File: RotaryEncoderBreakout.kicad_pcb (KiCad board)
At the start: 2 copper layers, 36 x 44.1 mm, 18 parts, among them J1 Conn_01x04_Male, J2 Conn_01x04_Male, J3 Conn_01x03_Male, SW1 RotaryEncoder_Switch_RGB, U1 WS2811

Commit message: Layout complete
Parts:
- removed R9: 0R, Resistors_SMD:R_0805_HandSoldering
- J1, J2: moved to F.Cu
- J3: value Conn_01x03_Male -> Conn_01x05_Male; footprint Pin_Headers:Pin_Header_Straight_1x03_Pitch2.54mm -> Pin_Headers:Pin_Header_Straight_1x05_Pitch2.54mm
- moved R7 15.6 mm to (135.9, 59.1)
- moved J1 7.65 mm to (113.7, 74.5)
- moved J2 7.65 mm to (113.7, 62.9)
- moved J3 4.58 mm to (137.2, 55.2), turned to 270 degrees
- moved C3 3.86 mm to (121.9, 59.1)
- moved R5 3.24 mm to (128.3, 84.5)
- moved SW1 2.92 mm to (132.1, 74.3)
- moved R6 2.62 mm to (118.1, 59.1), turned to 90 degrees
- moved R4 2.62 mm to (135.9, 84.5)
- moved U1 2.29 mm to (128.9, 61.0)
- moved R1 1.42 mm to (135.9, 63.5), turned to 0 degrees
- moved R2 1.27 mm to (121.9, 73.0), turned to 90 degrees
- moved R3 1.27 mm to (121.9, 79.4)
- moved R8 1.27 mm to (121.9, 66.7), turned to 90 degrees
- turned C1 to 270 degrees
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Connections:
- J1 pad 1: Net-(C4-Pad1) -> Net-(J1-Pad1)
- J1 pad 2: Net-(C1-Pad1) -> Net-(C2-Pad1)
- J1 pad 3: Net-(C2-Pad1) -> Net-(C1-Pad1)
- J1 pad 4: Net-(J1-Pad4) -> Net-(C4-Pad1)
- J2 pad 1: +5V -> Net-(J2-Pad1)
- J2 pad 4: Net-(J2-Pad4) -> +5V
- J3 pad 1: Net-(J3-Pad1) -> Net-(J1-Pad1)
- J3 pad 3: Net-(J1-Pad4) -> Net-(J3-Pad3)
- U1 pad 5: Net-(J3-Pad1) -> Net-(J3-Pad3)
- U1 pad 7: Net-(R9-Pad2) -> Net-(J3-Pad4)
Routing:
- net +5V: track 19.4 -> 95.6 mm, vias 1 -> 2
- net Net-(J1-Pad1): track 0.00 -> 50.7 mm
- net Net-(R3-Pad1): track 0.00 -> 21.7 mm
- net Net-(R1-Pad1): track 0.00 -> 18.2 mm, vias 0 -> 1
- net Net-(R2-Pad1): track 0.00 -> 13.5 mm
- net GND: track 0.00 -> 13.0 mm, vias 0 -> 7
- net Net-(C2-Pad1): track 0.00 -> 12.3 mm
- net Net-(J3-Pad1): track 10.6 -> 0.00 mm
- net Net-(C1-Pad1): track 0.00 -> 10.1 mm
- net Net-(C3-Pad2): track 0.00 -> 9.33 mm
- net Net-(C4-Pad1): track 0.00 -> 8.92 mm
- net Net-(SW1-Pad4): track 0.00 -> 7.38 mm
- net Net-(R7-Pad1): track 0.00 -> 7.01 mm
- net Net-(SW1-Pad2): track 0.00 -> 4.38 mm
- net Net-(SW1-Pad1): track 0.00 -> 4.08 mm
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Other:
- board size 36 x 44.1 mm -> 33 x 34.3 mm
- board text added: "5V"
- board text added: "GND"
- board text added: "PC0"
- board text added: "PC1"
- board text added: "PC2"
- board text added: "PC3"
- board text added: "Vin"

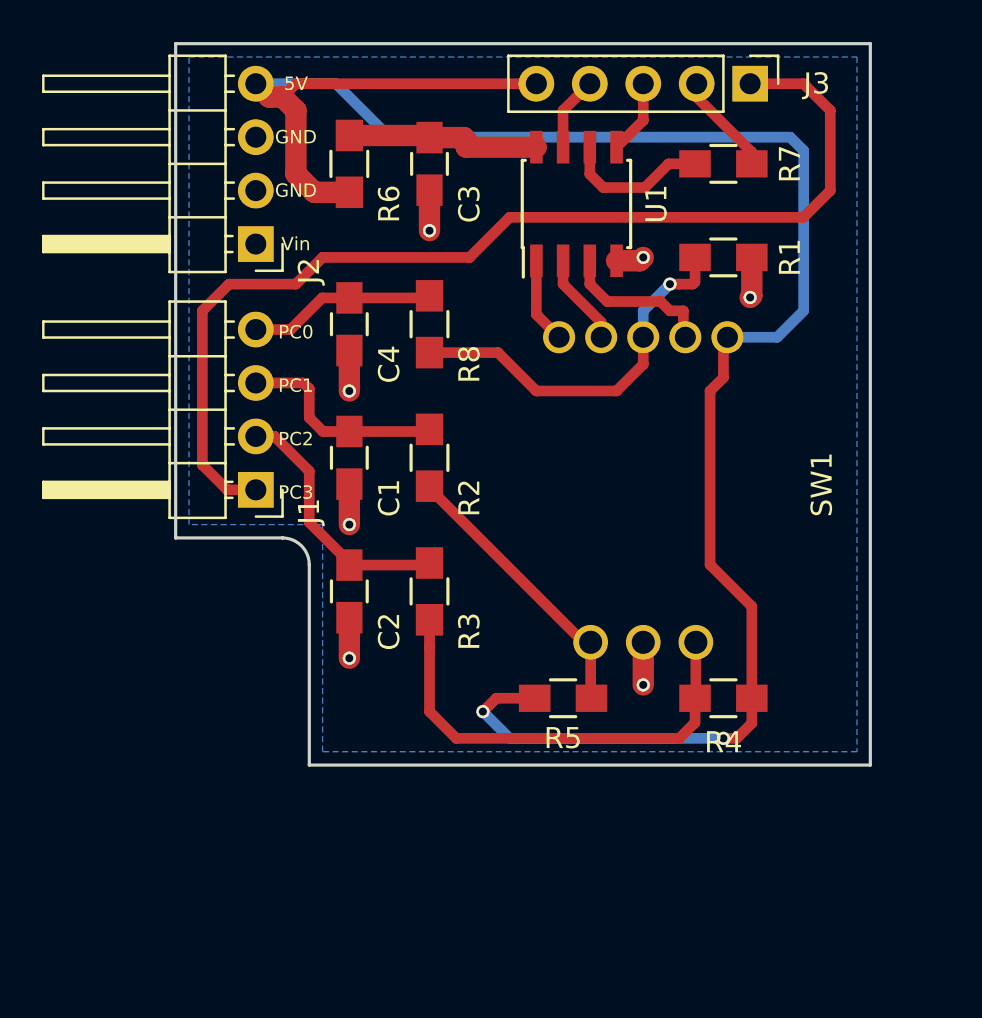
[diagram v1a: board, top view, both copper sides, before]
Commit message: Better silkscreen
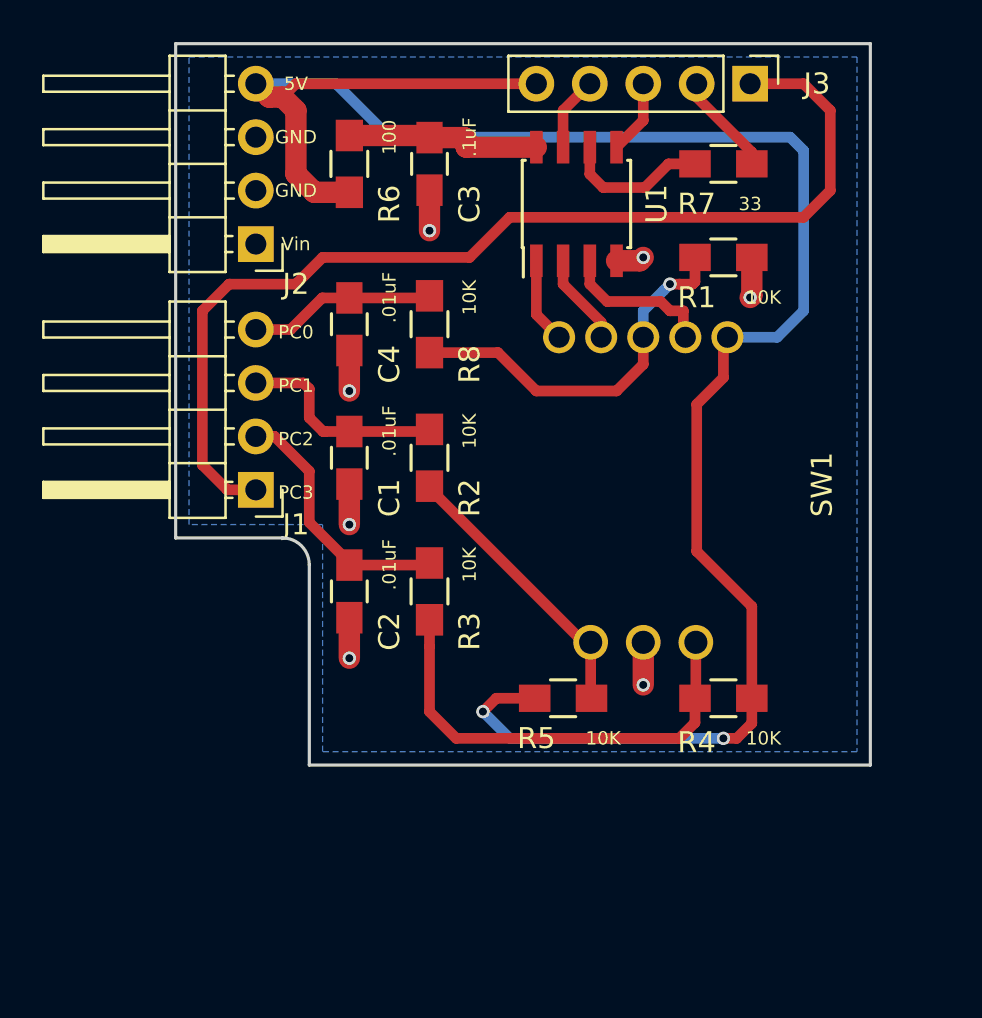
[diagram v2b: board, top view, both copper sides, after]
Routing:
- net +5V: track 95.6 -> 96.2 mm
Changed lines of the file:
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@@
     (47 F.CrtYd user)
     (48 B.Fab user)
-    (49 F.Fab user hide)
+    (49 F.Fab user)
   )
   (setup
@@
       (effects (font (size 1 1) (thickness 0.15)))
     )
-    (fp_text value .01uF (at -1.27 -1.905 270) (layer F.Fab)
-      (effects (font (size 1 1) (thickness 0.15)))
+    (fp_text value .01uF (at -1.27 -1.905 270) (layer F.SilkS)
+      (effects (font (size 0.635 0.635) (thickness 0.15)))
     )
     (fp_line (start -1 0.625) (end -1 -0.625) (layer F.Fab) (width 0.15))
@@
       (effects (font (size 1 1) (thickness 0.15)))
     )
-    (fp_text value .01uF (at -1.27 -1.905 270) (layer F.Fab)
-      (effects (font (size 1 1) (thickness 0.15)))
+    (fp_text value .01uF (at -1.27 -1.905 270) (layer F.SilkS)
+      (effects (font (size 0.635 0.635) (thickness 0.15)))
     )
     (fp_line (start -1 0.625) (end -1 -0.625) (layer F.Fab) (width 0.15))
@@
     (descr "Through hole angled pin header, 1x04, 2.54mm pitch, 6mm pin length, single row")
     (tags "Through hole angled pin header THT 1x04 2.54mm single row")
-    (fp_text reference J1 (at -2.54 -1.016 270) (layer F.SilkS)
+    (fp_text reference J1 (at -1.905 -1.651 360) (layer F.SilkS)
       (effects (font (size 1 1) (thickness 0.15)))
     )
@@
     (descr "Through hole angled pin header, 1x04, 2.54mm pitch, 6mm pin length, single row")
     (tags "Through hole angled pin header THT 1x04 2.54mm single row")
-    (fp_text reference J2 (at -2.54 -1.27 450) (layer F.SilkS)
+    (fp_text reference J2 (at -1.905 -1.905 180) (layer F.SilkS)
       (effects (font (size 1 1) (thickness 0.15)))
     )
@@
     (tags "resistor 0805")
     (attr smd)
-    (fp_text reference R1 (at 3.175 0 90) (layer F.SilkS)
-      (effects (font (size 1 1) (thickness 0.15)))
-    )
-    (fp_text value 10K (at 0 2.1) (layer F.Fab)
-      (effects (font (size 1 1) (thickness 0.15)))
+    (fp_text reference R1 (at -1.27 1.905 180) (layer F.SilkS)
+      (effects (font (size 1 1) (thickness 0.15)))
+    )
+    (fp_text value 10K (at 1.905 1.905) (layer F.SilkS)
+      (effects (font (size 0.635 0.635) (thickness 0.15)))
     )
     (fp_line (start -1 0.625) (end -1 -0.625) (layer F.Fab) (width 0.1))
@@
       (effects (font (size 1 1) (thickness 0.15)))
     )
-    (fp_text value 10K (at 1.27 1.905 90) (layer F.Fab)
-      (effects (font (size 1 1) (thickness 0.15)))
+    (fp_text value 10K (at 1.27 1.905 90) (layer F.SilkS)
+      (effects (font (size 0.635 0.635) (thickness 0.15)))
     )
     (fp_line (start -1 0.625) (end -1 -0.625) (layer F.Fab) (width 0.1))
@@
       (effects (font (size 1 1) (thickness 0.15)))
     )
-    (fp_text value 10K (at 1.27 1.905 90) (layer F.Fab)
-      (effects (font (size 1 1) (thickness 0.15)))
+    (fp_text value 10K (at 1.27 1.905 90) (layer F.SilkS)
+      (effects (font (size 0.635 0.635) (thickness 0.15)))
     )
     (fp_line (start -1 0.625) (end -1 -0.625) (layer F.Fab) (width 0.1))
@@
     (tags "resistor 0805")
     (attr smd)
-    (fp_text reference R4 (at 0 -2.1 180) (layer F.SilkS)
-      (effects (font (size 1 1) (thickness 0.15)))
-    )
-    (fp_text value 10K (at 0 2.1 180) (layer F.Fab)
-      (effects (font (size 1 1) (thickness 0.15)))
+    (fp_text reference R4 (at 1.27 -2.1 180) (layer F.SilkS)
+      (effects (font (size 1 1) (thickness 0.15)))
+    )
+    (fp_text value 10K (at -1.905 -1.905 180) (layer F.SilkS)
+      (effects (font (size 0.635 0.635) (thickness 0.15)))
     )
     (fp_line (start -1 0.625) (end -1 -0.625) (layer F.Fab) (width 0.1))
@@
     (tags "resistor 0805")
     (attr smd)
-    (fp_text reference R5 (at 0 1.905) (layer F.SilkS)
-      (effects (font (size 1 1) (thickness 0.15)))
-    )
-    (fp_text value 10K (at 0 2.1) (layer F.Fab)
-      (effects (font (size 1 1) (thickness 0.15)))
+    (fp_text reference R5 (at -1.27 1.905) (layer F.SilkS)
+      (effects (font (size 1 1) (thickness 0.15)))
+    )
+    (fp_text value 10K (at 1.905 1.905) (layer F.SilkS)
+      (effects (font (size 0.635 0.635) (thickness 0.15)))
     )
     (fp_line (start -1 0.625) (end -1 -0.625) (layer F.Fab) (width 0.1))
@@
       (effects (font (size 1 1) (thickness 0.15)))
     )
-    (fp_text value .1uF (at 1.27 1.905 90) (layer F.Fab)
-      (effects (font (size 1 1) (thickness 0.15)))
+    (fp_text value .1uF (at 1.27 1.905 90) (layer F.SilkS)
+      (effects (font (size 0.635 0.635) (thickness 0.15)))
     )
     (fp_line (start -1 0.625) (end -1 -0.625) (layer F.Fab) (width 0.15))
@@
       (effects (font (size 1 1) (thickness 0.15)))
     )
-    (fp_text value .01uF (at 1.27 1.905 270) (layer F.Fab)
-      (effects (font (size 1 1) (thickness 0.15)))
+    (fp_text value .01uF (at -1.27 -1.905 270) (layer F.SilkS)
+      (effects (font (size 0.635 0.635) (thickness 0.15)))
     )
     (fp_line (start -1 0.625) (end -1 -0.625) (layer F.Fab) (width 0.15))
@@
       (effects (font (size 1 1) (thickness 0.15)))
     )
-    (fp_text value 100 (at 0 2.1 90) (layer F.Fab)
-      (effects (font (size 1 1) (thickness 0.15)))
+    (fp_text value 100 (at 1.27 1.905 90) (layer F.SilkS)
+      (effects (font (size 0.635 0.635) (thickness 0.15)))
     )
     (fp_line (start -1 0.625) (end -1 -0.625) (layer F.Fab) (width 0.1))
@@
     (tags "resistor 0805")
     (attr smd)
-    (fp_text reference R7 (at 3.175 0 270) (layer F.SilkS)
-      (effects (font (size 1 1) (thickness 0.15)))
-    )
-    (fp_text value 33 (at 5.08 -0.455 90) (layer F.Fab)
-      (effects (font (size 1 1) (thickness 0.15)))
+    (fp_text reference R7 (at -1.27 1.905) (layer F.SilkS)
+      (effects (font (size 1 1) (thickness 0.15)))
+    )
+    (fp_text value 33 (at 1.27 1.905) (layer F.SilkS)
+      (effects (font (size 0.635 0.635) (thickness 0.15)))
     )
     (fp_line (start -1 0.625) (end -1 -0.625) (layer F.Fab) (width 0.1))
@@
       (effects (font (size 1 1) (thickness 0.15)))
     )
-    (fp_text value 10K (at -1.27 -1.905 90) (layer F.Fab)
-      (effects (font (size 1 1) (thickness 0.15)))
+    (fp_text value 10K (at 1.27 1.905 90) (layer F.SilkS)
+      (effects (font (size 0.635 0.635) (thickness 0.15)))
     )
     (fp_line (start -1 0.625) (end -1 -0.625) (layer F.Fab) (width 0.1))
@@
   (segment (start 118.11 78.125) (end 121.82 78.125) (width 0.508) (layer F.Cu) (net 3))
   (segment (start 121.82 78.125) (end 121.92 78.025) (width 0.508) (layer F.Cu) (net 3))
+  (segment (start 137.24 84.455) (end 137.24 80.09) (width 0.508) (layer F.Cu) (net 4))
+  (segment (start 137.24 80.09) (end 134.62 77.47) (width 0.508) (layer F.Cu) (net 4))
+  (segment (start 134.62 77.47) (end 134.62 70.485) (width 0.508) (layer F.Cu) (net 4))
+  (segment (start 134.62 70.485) (end 135.89 69.215) (width 0.508) (layer F.Cu) (net 4))
+  (segment (start 135.89 69.215) (end 135.89 67.485) (width 0.508) (layer F.Cu) (net 4))
+  (segment (start 135.89 67.485) (end 136.08 67.295) (width 0.508) (layer F.Cu) (net 4))
   (segment (start 113.665 55.245) (end 117.475 55.245) (width 0.508) (layer B.Cu) (net 4))
   (segment (start 117.475 55.245) (end 120.015 57.785) (width 0.508) (layer B.Cu) (net 4))
@@
   (segment (start 139.7 66.04) (end 138.445 67.295) (width 0.508) (layer B.Cu) (net 4))
   (segment (start 138.445 67.295) (end 136.08 67.295) (width 0.508) (layer B.Cu) (net 4))
-  (segment (start 137.24 84.455) (end 137.24 80.09) (width 0.508) (layer F.Cu) (net 4))
-  (segment (start 137.24 80.09) (end 135.255 78.105) (width 0.508) (layer F.Cu) (net 4))
-  (segment (start 135.255 78.105) (end 135.255 69.85) (width 0.508) (layer F.Cu) (net 4))
-  (segment (start 135.255 69.85) (end 135.89 69.215) (width 0.508) (layer F.Cu) (net 4))
-  (segment (start 135.89 67.485) (end 136.08 67.295) (width 0.508) (layer F.Cu) (net 4))
-  (segment (start 135.89 69.215) (end 135.89 67.485) (width 0.508) (layer F.Cu) (net 4))
   (segment (start 136.525 86.36) (end 137.24 85.645) (width 0.508) (layer F.Cu) (net 4))
   (segment (start 137.24 85.645) (end 137.24 85.613) (width 0.508) (layer F.Cu) (net 4))
@@
   (segment (start 133.985 66.04) (end 133.985 67.2) (width 0.508) (layer F.Cu) (net 9))
   (segment (start 123.665 58.26) (end 123.665 57.909) (width 1.016) (layer F.Cu) (net 10))
+  (segment (start 127 58.26) (end 123.665 58.26) (width 1.016) (layer F.Cu) (net 10))
+  (segment (start 123.665 57.909) (end 123.561 57.805) (width 1.016) (layer F.Cu) (net 10))
   (segment (start 123.561 57.805) (end 121.92 57.805) (width 1.016) (layer F.Cu) (net 10))
-  (segment (start 123.665 57.909) (end 123.561 57.805) (width 1.016) (layer F.Cu) (net 10))
-  (segment (start 127 58.26) (end 123.665 58.26) (width 1.016) (layer F.Cu) (net 10))
   (segment (start 118.11 57.705) (end 121.82 57.705) (width 1.016) (layer F.Cu) (net 10))
   (segment (start 121.82 57.705) (end 121.92 57.805) (width 1.016) (layer F.Cu) (net 10))

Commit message: Final layout
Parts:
- J1, J2: footprint Pin_Headers:Pin_Header_Angled_1x04_Pitch2.54mm -> Pin_Headers:Pin_Header_Straight_1x04_Pitch2.54mm; moved to B.Cu
- moved J1 1.02 mm to (113.7, 75.6), turned to 0 degrees
- turned J2 to 0 degrees
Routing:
- net Net-(C1-Pad1): track 10.1 -> 8.83 mm
- net Net-(J1-Pad1): track 50.7 -> 51.7 mm
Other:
- outline, holes or cut-outs redrawn
- board text added: "EC12PLRGB Rotary Encoder Breakout Carl Raymond Dec. 2017"
- board text added: "J3: Din=2 Dout=3 Short 1-2 for Din=PC3 Short 4-5 for 400KHz / Open for 800KHz"

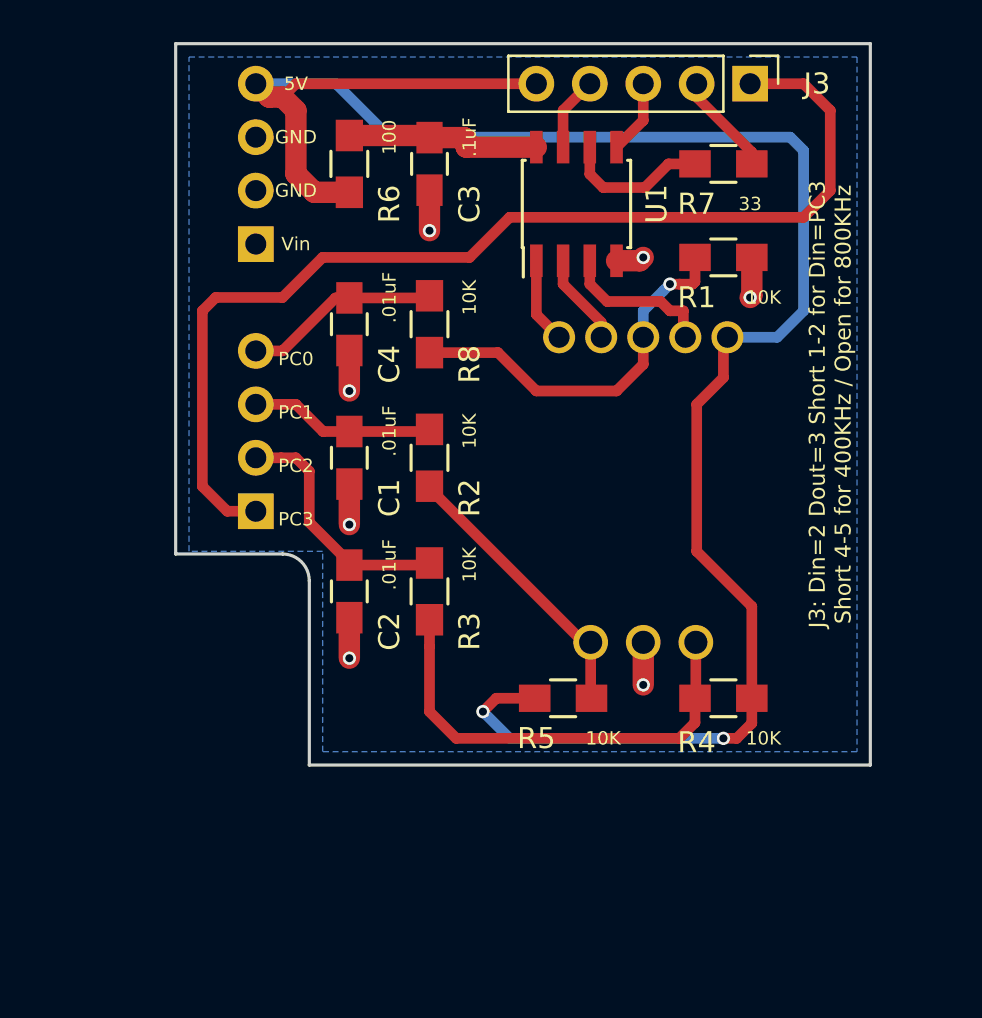
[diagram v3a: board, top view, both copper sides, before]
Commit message: Changed symbol and library references to local copy
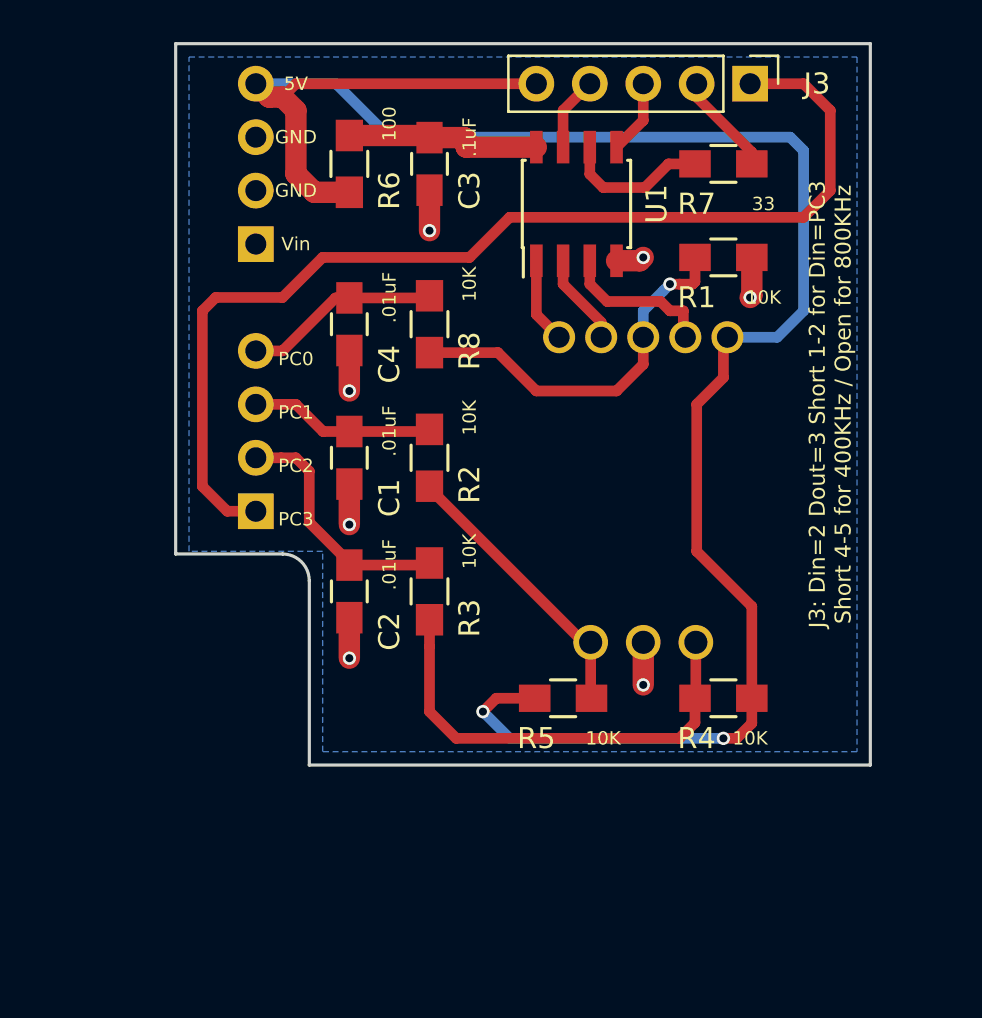
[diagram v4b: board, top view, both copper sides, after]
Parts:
- C1, C2, C3, C4: footprint Capacitors_SMD:C_0805_HandSoldering -> lib_fp:C_0805_HandSoldering
- J1, J2: footprint Pin_Headers:Pin_Header_Straight_1x04_Pitch2.54mm -> lib_fp:Pin_Header_Straight_1x04_Pitch2.54mm
- J3: footprint Pin_Headers:Pin_Header_Straight_1x05_Pitch2.54mm -> lib_fp:Pin_Header_Straight_1x05_Pitch2.54mm
- R1, R2, R3, R4, R5, R6, R7, R8: footprint Resistors_SMD:R_0805_HandSoldering -> lib_fp:R_0805_HandSoldering
- U1: footprint Housings_SOIC:SOIC-8_3.9x4.9mm_Pitch1.27mm -> lib_fp:SOIC-8_3.9x4.9mm_Pitch1.27mm
